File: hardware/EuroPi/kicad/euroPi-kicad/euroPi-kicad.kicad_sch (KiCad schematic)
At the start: 119 parts, among them J1 Output 1 Jack, J10 Eurorack Power 2x8 16p, J11 Conn_01x13_Socket, J12 OLED 64x128, J13 USB_B_Micro, J14 Conn_01x03_Pin, J15 Conn_01x04_Pin, J16 Conn_02x04_Top_Bottom, J17 Conn_01x13_Pin, J18 Conn_01x04_Pin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

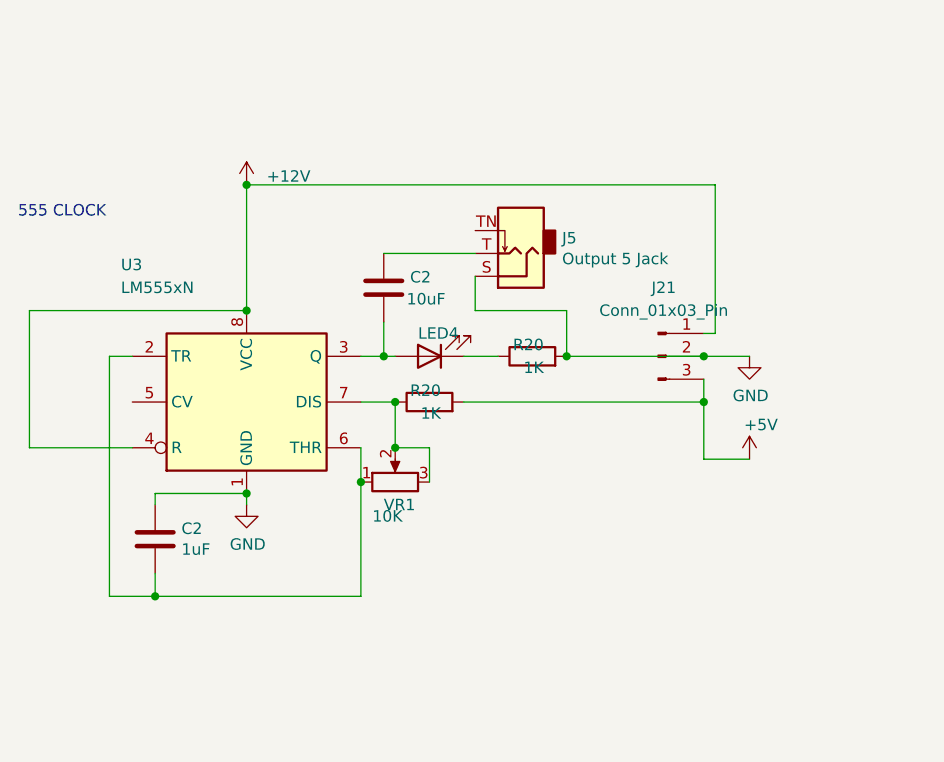
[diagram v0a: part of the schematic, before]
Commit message: euroPI base minor fixes incl adding ground plane
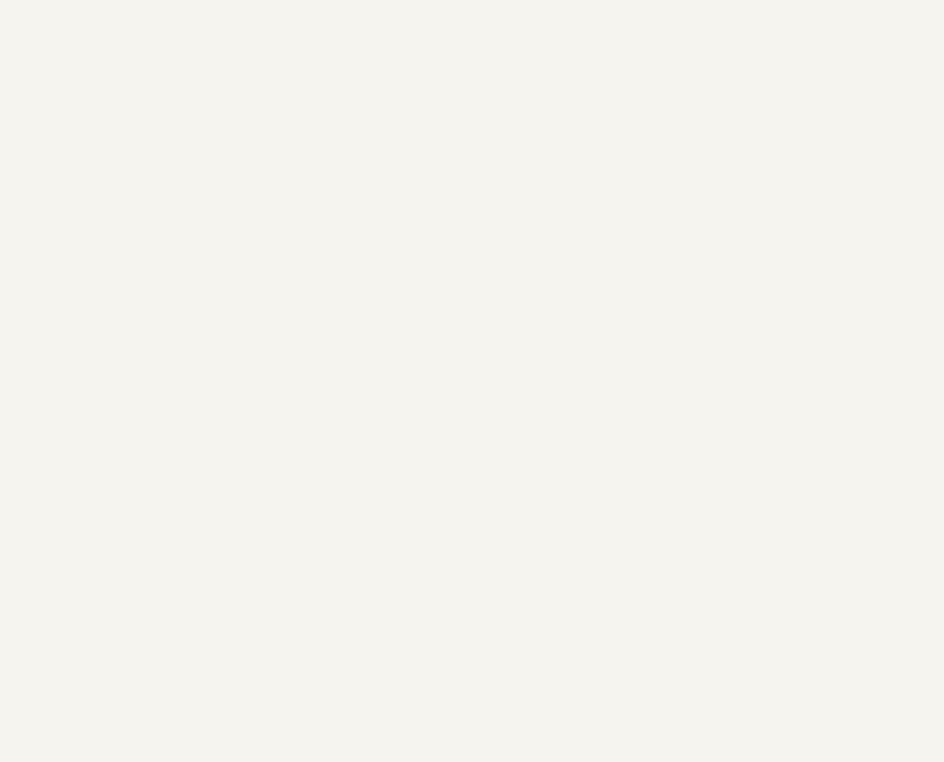
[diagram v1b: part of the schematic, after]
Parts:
- removed C2: 10uF, Capacitor_THT:C_Radial_D5.0mm_H11.0mm_P2.00mm, symbol Device:C
- removed C2: 1uF, Capacitor_THT:C_Radial_D5.0mm_H11.0mm_P2.00mm, symbol Device:C
- removed J21: Conn_01x03_Pin, Connector_PinSocket_2.54mm:PinSocket_1x03_P2.54mm_Vertical, symbol Connector:Conn_01x03_Pin
- removed J5: Output 5 Jack, Connector_Audio:Jack_3.5mm_QingPu_WQP-PJ398SM_Vertical_CircularHoles, symbol Connector:AudioJack2_SwitchT
- removed LED4: LED, LED_THT:LED_D1.8mm_W3.3mm_H2.4mm, symbol Device:LED
- removed R20 (x2): 1K, Resistor_THT:R_Axial_DIN0207_L6.3mm_D2.5mm_P5.08mm_Vertical, symbol Device:R
- removed Reference?: +12V, symbol text:TEXT
- removed U3: LM555xN, Package_DIP:DIP-8_W7.62mm, symbol Timer:LM555xN
- removed VR1: 10K, Potentiometer_THT:Potentiometer_Bourns_PTV09A-1_Single_Vertical, symbol Device:R_POT
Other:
- note removed: "555 CLOCK"

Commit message: small fixes added missed net and text around eurorack conn
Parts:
- added H1, H2, H3, H4: MountingHole_Pad, MountingHole:MountingHole_2.7mm_M2.5_ISO14580_Pad_TopBottom, symbol Mechanical:MountingHole_Pad
- C1, C2: value 1uF -> 1uF (Polarised); footprint Capacitor_THT:C_Radial_D5.0mm_H11.0mm_P2.00mm -> Capacitor_THT:CP_Radial_D5.0mm_P2.00mm
- C15, C16: value 10uF -> 10uF (Polarised); footprint Capacitor_THT:C_Radial_D5.0mm_H11.0mm_P2.00mm -> Capacitor_THT:CP_Radial_D5.0mm_P2.00mm
- D1, D2, D3, D4: value ${SIM.PARAMS} -> 1N5817 Schottky Diode; footprint Diode_THT:D_A-405_P2.54mm_Vertical_KathodeUp -> Diode_THT:D_DO-41_SOD81_P2.54mm_Vertical_KathodeUp
- J11: value Conn_01x13_Socket -> Conn_01x12_Socket; footprint Connector_PinSocket_2.54mm:PinSocket_1x13_P2.54mm_Vertical -> Connector_PinSocket_2.54mm:PinSocket_1x12_P2.54mm_Vertical; symbol Connector:Conn_01x13_Socket -> Connector:Conn_01x12_Socket
- J17: value Conn_01x13_Pin -> Conn_01x12_Pin; footprint Connector_PinSocket_2.54mm:PinSocket_1x13_P2.54mm_Vertical -> Connector_PinHeader_2.54mm:PinHeader_1x12_P2.54mm_Vertical; symbol Connector:Conn_01x13_Pin -> Connector:Conn_01x12_Pin
- O, O? (x8): footprint Package_DIP:DIP-14_W7.62mm_Socket -> Library:DIP-14_W7.62mm_Socket_gap_in_the_middle
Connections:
- net GND: now also H1.1, H2.1, H3.1, H4.1; no longer J11.13 (Pin_13), J17.13 (Pin_13)
